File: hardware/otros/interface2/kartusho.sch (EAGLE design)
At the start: 9 parts, among them IC1 74HC164N, IC3 74HC32N, U1 AM29F040S

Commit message: 
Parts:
- removed U$1: IF2BUS, SPECTRUM:IF2BUS
- added U$2: IF2BUSMINI, SPECTRUM:IF2BUSMINI
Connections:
- net A0: now also U$2.A0; no longer U$1.A0
- net A1: now also U$2.A1; no longer U$1.A1
- net A10: now also U$2.A10; no longer U$1.A10
- net A11: now also U$2.A11; no longer U$1.A11
- net A12: now also U$2.A12; no longer U$1.A12
- net A13: now also U$2.A13; no longer U$1.A13
- net A14: now also U$2.A14; no longer U$1.A14
- net A15: now also U$2.A15; no longer U$1.A15
- net A2: now also U$2.A2; no longer U$1.A2
- net A3: now also U$2.A3; no longer U$1.A3
- net A4: now also U$2.A4; no longer U$1.A4
- net A5: now also U$2.A5; no longer U$1.A5
- net A6: now also U$2.A6; no longer U$1.A6
- net A7: now also U$2.A7; no longer U$1.A7
- net A8: now also U$2.A8; no longer U$1.A8
- net A9: now also U$2.A9; no longer U$1.A9
- net D0: now also U$2.D0; no longer U$1.D0
- net D1: now also U$2.D1; no longer U$1.D1
- net D2: now also U$2.D2; no longer U$1.D2
- net D3: now also U$2.D3; no longer U$1.D3
- net D4: now also U$2.D4; no longer U$1.D4
- net D5: now also U$2.D5; no longer U$1.D5
- net D6: now also U$2.D6; no longer U$1.D6
- net D7: now also U$2.D7; no longer U$1.D7
- net GND: now also U$2.GND; no longer U$1.GND
- net MREQ: now also U$2.MEMREQ; no longer U$1.MEMREQ
- net RD: now also U$2.RD; no longer U$1.RD
- net VCC: now also U$2.+5V, U$2.ROMCS; no longer U$1.+5V, U$1.ROMCS
- net WR: now also U$2.WR; no longer U$1.WR
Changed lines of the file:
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@@
 </classes>
 <parts>
-<part name="U$1" library="SPECTRUM" deviceset="IF2BUS" device=""/>
 <part name="C1" library="rcl" deviceset="C-EU" device="050-025X075" value="100nF"/>
 <part name="IC1" library="74xx-us" deviceset="74*164" device="N" technology="HC"/>
@@
 <part name="GND1" library="supply1" deviceset="GND" device=""/>
 <part name="P+1" library="supply1" deviceset="VCC" device=""/>
+<part name="U$2" library="SPECTRUM" deviceset="IF2BUSMINI" device=""/>
 </parts>
 <sheets>
@@
 </plain>
 <instances>
-<instance part="U$1" gate="G$1" x="-10.16" y="60.96"/>
 <instance part="C1" gate="G$1" x="10.16" y="93.98"/>
 <instance part="IC1" gate="A" x="50.8" y="48.26"/>
@@
 <instance part="GND1" gate="1" x="10.16" y="83.82"/>
 <instance part="P+1" gate="VCC" x="10.16" y="101.6"/>
+<instance part="U$2" gate="G$1" x="-10.16" y="60.96"/>
 </instances>
 <busses>
@@
 <wire x1="-15.24" y1="88.9" x2="-7.62" y2="88.9" width="0.1524" layer="91"/>
 <label x="-10.16" y="88.9" size="1.778" layer="95"/>
-<pinref part="U$1" gate="G$1" pin="D0"/>
+<pinref part="U$2" gate="G$1" pin="D0"/>
 </segment>
 <segment>
@@
 <wire x1="-15.24" y1="83.82" x2="-7.62" y2="83.82" width="0.1524" layer="91"/>
 <label x="-10.16" y="83.82" size="1.778" layer="95"/>
-<pinref part="U$1" gate="G$1" pin="D1"/>
+<pinref part="U$2" gate="G$1" pin="D1"/>
 </segment>
 <segment>
@@
 <wire x1="-15.24" y1="78.74" x2="-7.62" y2="78.74" width="0.1524" layer="91"/>
 <label x="-10.16" y="78.74" size="1.778" layer="95"/>
-<pinref part="U$1" gate="G$1" pin="D2"/>
+<pinref part="U$2" gate="G$1" pin="D2"/>
 </segment>
 <segment>
@@
 <wire x1="-15.24" y1="73.66" x2="-7.62" y2="73.66" width="0.1524" layer="91"/>
 <label x="-10.16" y="73.66" size="1.778" layer="95"/>
-<pinref part="U$1" gate="G$1" pin="D3"/>
+<pinref part="U$2" gate="G$1" pin="D3"/>
 </segment>
 <segment>
@@
 <wire x1="-15.24" y1="68.58" x2="-7.62" y2="68.58" width="0.1524" layer="91"/>
 <label x="-10.16" y="68.58" size="1.778" layer="95"/>
-<pinref part="U$1" gate="G$1" pin="D4"/>
+<pinref part="U$2" gate="G$1" pin="D4"/>
 </segment>
 <segment>
@@
 <wire x1="-15.24" y1="63.5" x2="-7.62" y2="63.5" width="0.1524" layer="91"/>
 <label x="-10.16" y="63.5" size="1.778" layer="95"/>
-<pinref part="U$1" gate="G$1" pin="D5"/>
+<pinref part="U$2" gate="G$1" pin="D5"/>
 </segment>
 <segment>
@@
 <wire x1="-15.24" y1="58.42" x2="-7.62" y2="58.42" width="0.1524" layer="91"/>
 <label x="-10.16" y="58.42" size="1.778" layer="95"/>
-<pinref part="U$1" gate="G$1" pin="D6"/>
+<pinref part="U$2" gate="G$1" pin="D6"/>
 </segment>
 <segment>
@@
 <wire x1="-15.24" y1="53.34" x2="-7.62" y2="53.34" width="0.1524" layer="91"/>
 <label x="-10.16" y="53.34" size="1.778" layer="95"/>
-<pinref part="U$1" gate="G$1" pin="D7"/>
+<pinref part="U$2" gate="G$1" pin="D7"/>
 </segment>
 <segment>
@@
 <wire x1="-53.34" y1="88.9" x2="-45.72" y2="88.9" width="0.1524" layer="91"/>
 <label x="-53.34" y="88.9" size="1.778" layer="95"/>
-<pinref part="U$1" gate="G$1" pin="A0"/>
+<pinref part="U$2" gate="G$1" pin="A0"/>
 </segment>
 <segment>
@@
 <wire x1="-53.34" y1="83.82" x2="-45.72" y2="83.82" width="0.1524" layer="91"/>
 <label x="-53.34" y="83.82" size="1.778" layer="95"/>
-<pinref part="U$1" gate="G$1" pin="A1"/>
+<pinref part="U$2" gate="G$1" pin="A1"/>
 </segment>
 <segment>
@@
 <wire x1="-53.34" y1="78.74" x2="-45.72" y2="78.74" width="0.1524" layer="91"/>
 <label x="-53.34" y="78.74" size="1.778" layer="95"/>
-<pinref part="U$1" gate="G$1" pin="A2"/>
+<pinref part="U$2" gate="G$1" pin="A2"/>
 </segment>
 <segment>
@@
 <wire x1="-53.34" y1="73.66" x2="-45.72" y2="73.66" width="0.1524" layer="91"/>
 <label x="-53.34" y="73.66" size="1.778" layer="95"/>
-<pinref part="U$1" gate="G$1" pin="A3"/>
+<pinref part="U$2" gate="G$1" pin="A3"/>
 </segment>
 <segment>
@@
 <wire x1="-53.34" y1="68.58" x2="-45.72" y2="68.58" width="0.1524" layer="91"/>
 <label x="-53.34" y="68.58" size="1.778" layer="95"/>
-<pinref part="U$1" gate="G$1" pin="A4"/>
+<pinref part="U$2" gate="G$1" pin="A4"/>
 </segment>
 <segment>
@@
 <wire x1="-53.34" y1="63.5" x2="-45.72" y2="63.5" width="0.1524" layer="91"/>
 <label x="-53.34" y="63.5" size="1.778" layer="95"/>
-<pinref part="U$1" gate="G$1" pin="A5"/>
+<pinref part="U$2" gate="G$1" pin="A5"/>
 </segment>
 <segment>
@@
 <wire x1="-53.34" y1="58.42" x2="-45.72" y2="58.42" width="0.1524" layer="91"/>
 <label x="-53.34" y="58.42" size="1.778" layer="95"/>
-<pinref part="U$1" gate="G$1" pin="A6"/>
+<pinref part="U$2" gate="G$1" pin="A6"/>
 </segment>
 <segment>
@@
 <wire x1="-53.34" y1="53.34" x2="-45.72" y2="53.34" width="0.1524" layer="91"/>
 <label x="-53.34" y="53.34" size="1.778" layer="95"/>
-<pinref part="U$1" gate="G$1" pin="A7"/>
+<pinref part="U$2" gate="G$1" pin="A7"/>
 </segment>
 <segment>
@@
 <wire x1="-53.34" y1="48.26" x2="-45.72" y2="48.26" width="0.1524" layer="91"/>
 <label x="-53.34" y="48.26" size="1.778" layer="95"/>
-<pinref part="U$1" gate="G$1" pin="A8"/>
+<pinref part="U$2" gate="G$1" pin="A8"/>
 </segment>
 <segment>
@@
 <wire x1="-53.34" y1="43.18" x2="-45.72" y2="43.18" width="0.1524" layer="91"/>
 <label x="-53.34" y="43.18" size="1.778" layer="95"/>
-<pinref part="U$1" gate="G$1" pin="A9"/>
+<pinref part="U$2" gate="G$1" pin="A9"/>
 </segment>
 <segment>
@@
 <wire x1="-53.34" y1="38.1" x2="-45.72" y2="38.1" width="0.1524" layer="91"/>
 <label x="-53.34" y="38.1" size="1.778" layer="95"/>
-<pinref part="U$1" gate="G$1" pin="A10"/>
+<pinref part="U$2" gate="G$1" pin="A10"/>
 </segment>
 <segment>
@@
 <wire x1="-53.34" y1="33.02" x2="-45.72" y2="33.02" width="0.1524" layer="91"/>
 <label x="-53.34" y="33.02" size="1.778" layer="95"/>
-<pinref part="U$1" gate="G$1" pin="A11"/>
+<pinref part="U$2" gate="G$1" pin="A11"/>
 </segment>
 <segment>
@@
 <wire x1="-53.34" y1="27.94" x2="-45.72" y2="27.94" width="0.1524" layer="91"/>
 <label x="-53.34" y="27.94" size="1.778" layer="95"/>
-<pinref part="U$1" gate="G$1" pin="A12"/>
+<pinref part="U$2" gate="G$1" pin="A12"/>
 </segment>
 <segment>
@@
 <wire x1="-53.34" y1="22.86" x2="-45.72" y2="22.86" width="0.1524" layer="91"/>
 <label x="-53.34" y="22.86" size="1.778" layer="95"/>
-<pinref part="U$1" gate="G$1" pin="A13"/>
+<pinref part="U$2" gate="G$1" pin="A13"/>
 </segment>
 <segment>
@@
 <wire x1="-53.34" y1="17.78" x2="-45.72" y2="17.78" width="0.1524" layer="91"/>
 <label x="-53.34" y="17.78" size="1.778" layer="95"/>
-<pinref part="U$1" gate="G$1" pin="A14"/>
+<pinref part="U$2" gate="G$1" pin="A14"/>
 </segment>
 <segment>
@@
 <wire x1="-53.34" y1="12.7" x2="-45.72" y2="12.7" width="0.1524" layer="91"/>
 <label x="-53.34" y="12.7" size="1.778" layer="95"/>
-<pinref part="U$1" gate="G$1" pin="A15"/>
+<pinref part="U$2" gate="G$1" pin="A15"/>
 </segment>
 <segment>
@@
 <wire x1="-15.24" y1="48.26" x2="-7.62" y2="48.26" width="0.1524" layer="91"/>
 <label x="-10.16" y="48.26" size="1.778" layer="95"/>
-<pinref part="U$1" gate="G$1" pin="MEMREQ"/>
+<pinref part="U$2" gate="G$1" pin="MEMREQ"/>
 </segment>
 <segment>
@@
 <wire x1="-15.24" y1="33.02" x2="-7.62" y2="33.02" width="0.1524" layer="91"/>
 <label x="-10.16" y="33.02" size="1.778" layer="95"/>
-<pinref part="U$1" gate="G$1" pin="GND"/>
+<pinref part="U$2" gate="G$1" pin="GND"/>
 </segment>
 <segment>
@@
 <wire x1="-7.62" y1="38.1" x2="-5.08" y2="38.1" width="0.1524" layer="91"/>
 <junction x="-7.62" y="38.1"/>
-<pinref part="U$1" gate="G$1" pin="+5V"/>
-<pinref part="U$1" gate="G$1" pin="ROMCS"/>
+<pinref part="U$2" gate="G$1" pin="+5V"/>
+<pinref part="U$2" gate="G$1" pin="ROMCS"/>
 </segment>
 <segment>
@@
 <wire x1="-15.24" y1="27.94" x2="-7.62" y2="27.94" width="0.1524" layer="91"/>
 <label x="-10.16" y="27.94" size="1.778" layer="95"/>
-<pinref part="U$1" gate="G$1" pin="RD"/>
+<pinref part="U$2" gate="G$1" pin="RD"/>
 </segment>
 </net>
@@
 <wire x1="-15.24" y1="22.86" x2="-7.62" y2="22.86" width="0.1524" layer="91"/>
 <label x="-10.16" y="22.86" size="1.778" layer="95"/>
-<pinref part="U$1" gate="G$1" pin="WR"/>
-</segment>
-<segment>
+<pinref part="U$2" gate="G$1" pin="WR"/>
+</segment>
+<segment>

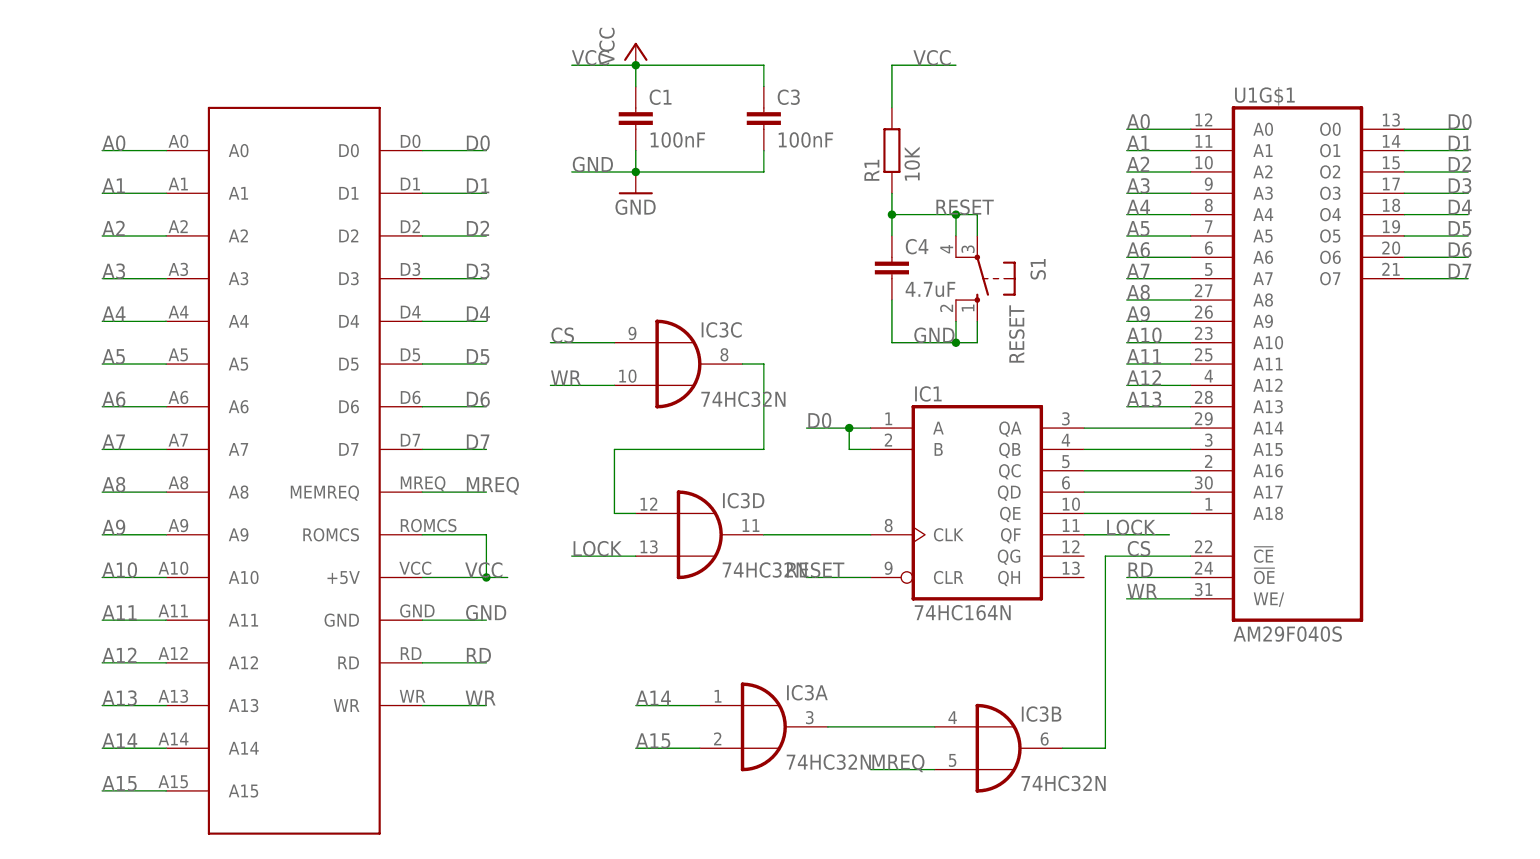
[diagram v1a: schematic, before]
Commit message: 
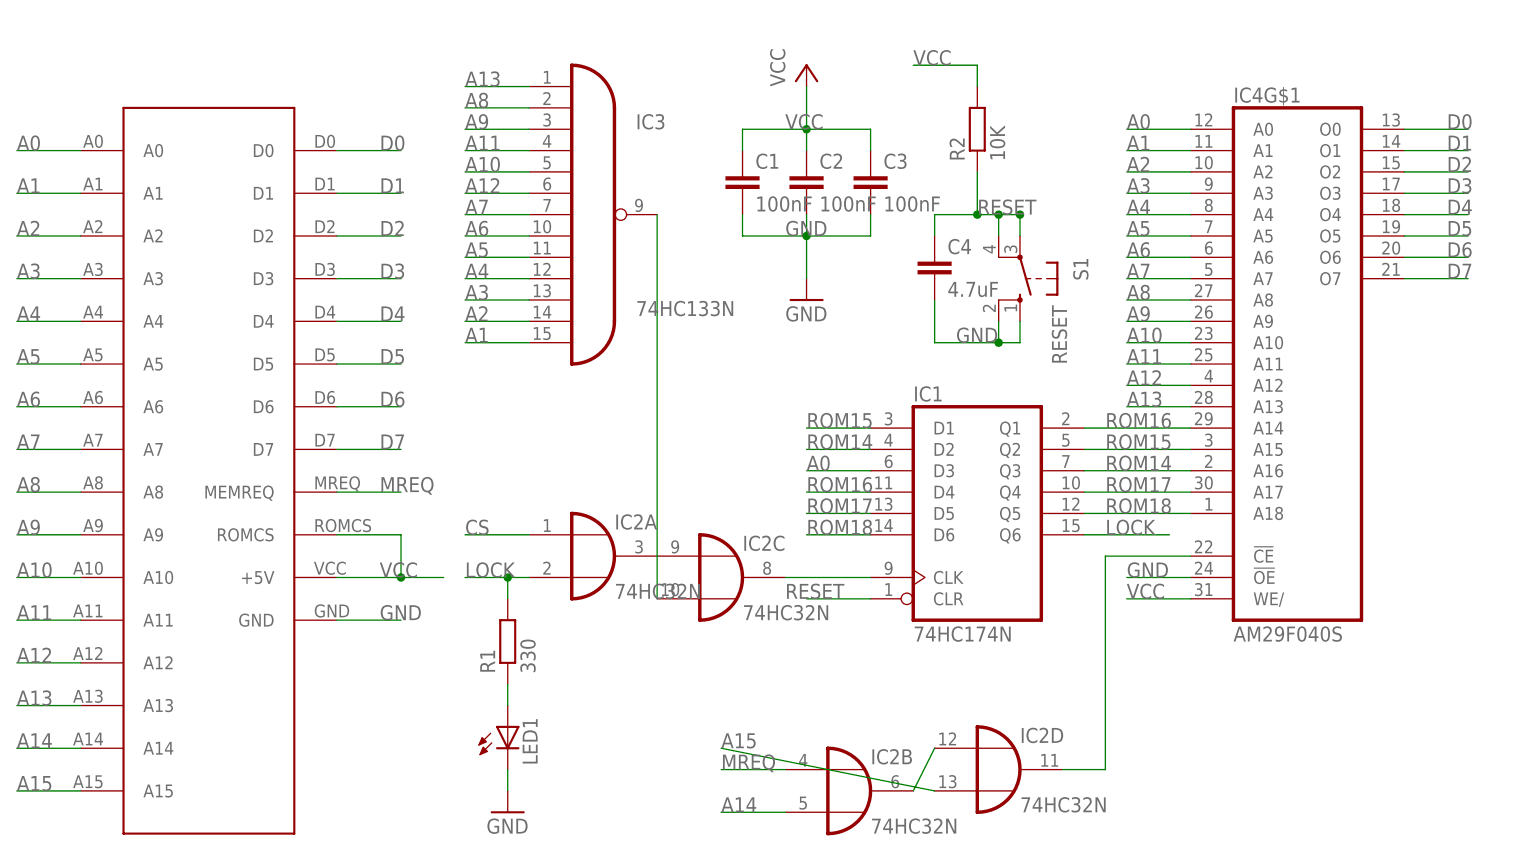
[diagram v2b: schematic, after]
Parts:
- removed U$2: IF2BUSMINI, SPECTRUM:IF2BUSMINI
- added C2: 100nF, rcl:C-EU025-025X050
- added IC2: 74HC32N, 74xx-eu:74HC32N
- added LED1: (no value), led:LED3MM
- added R2: 10K, rcl:R-EU_0204/7
- added U$1: IF2BUS, SPECTRUM:IF2BUS
- C1, C3, C4: device rcl:C-EU050-025X075 -> rcl:C-EU025-025X050
- IC1: value 74HC164N -> 74HC174N; device 74xx-us:74HC164N -> 74xx-eu:74HC174N
- IC3: value 74HC32N -> 74HC133N; device 74xx-eu:74HC32N -> 74xx-eu:74HC133N
- R1: value 10K -> 330
- renumbered U1 to IC4
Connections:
- removed net N$10: IC1A.CLK, IC3D.O
- removed net N$11: IC3C.O, IC3D.I0
- removed net N$5: IC1A.QB, IC4G$1.A15
- removed net N$6: IC1A.QA, IC4G$1.A14
- removed net RD: IC4G$1.!OE, U$2.RD
- removed net WR: IC3C.I1, IC4G$1.WE/, U$2.WR
- new net N$1: IC1A.CLK, IC2C.O
- new net ROM14: IC1A.D2, IC1A.Q3, IC4G$1.A16
- new net ROM15: IC1A.D1, IC1A.Q2, IC4G$1.A15
- new net ROM16: IC1A.D4, IC1A.Q1, IC4G$1.A14
- new net ROM17: IC1A.D5, IC1A.Q4, IC4G$1.A17
- new net ROM18: IC1A.D6, IC1A.Q5, IC4G$1.A18
- net A0: now also IC1A.D3, U$1.A0; no longer U$2.A0
- net A1: now also IC3A.I12, U$1.A1; no longer U$2.A1
- net A10: now also IC3A.I4, U$1.A10; no longer U$2.A10
- net A11: now also IC3A.I3, U$1.A11; no longer U$2.A11
- net A12: now also IC3A.I5, U$1.A12; no longer U$2.A12
- net A13: now also IC3A.I0, U$1.A13; no longer U$2.A13
- net A14: now also IC2B.I1, U$1.A14; no longer IC3A.I0, U$2.A14
- net A15: now also IC2D.I1, U$1.A15; no longer IC3A.I1, U$2.A15
- net A2: now also IC3A.I11, U$1.A2; no longer U$2.A2
- net A3: now also IC3A.I10, U$1.A3; no longer U$2.A3
- net A4: now also IC3A.I9, U$1.A4; no longer U$2.A4
- net A5: now also IC3A.I8, U$1.A5; no longer U$2.A5
- net A6: now also IC3A.I7, U$1.A6; no longer U$2.A6
- net A7: now also IC3A.I6, U$1.A7; no longer U$2.A7
- net A8: now also IC3A.I1, U$1.A8; no longer U$2.A8
- net A9: now also IC3A.I2, U$1.A9; no longer U$2.A9
- net CS: now also IC2A.I0, IC2D.O; no longer IC3B.O, IC3C.I0
- net D0: now also U$1.D0; no longer IC1A.A, IC1A.B, U$2.D0
- net D1: now also U$1.D1; no longer U$2.D1
- net D2: now also U$1.D2; no longer U$2.D2
- net D3: now also U$1.D3; no longer U$2.D3
- net D4: now also U$1.D4; no longer U$2.D4
- net D5: now also U$1.D5; no longer U$2.D5
- net D6: now also U$1.D6; no longer U$2.D6
- net D7: now also U$1.D7; no longer U$2.D7
- net GND: now also C2.2, IC4G$1.!OE, LED1.C, U$1.GND; no longer U$2.GND
- net LOCK: now also IC1A.Q6, IC2A.I1, R1.2; no longer IC1A.QF, IC3D.I1
- net MREQ: now also IC2B.I0, U$1.MEMREQ; no longer IC3B.I1, U$2.MEMREQ
- net N$2: now also IC2B.O, IC2D.I0; no longer IC1A.QE, IC4G$1.A18
- net N$3: now also IC2A.O, IC2C.I0; no longer IC1A.QD, IC4G$1.A17
- net N$4: now also IC2C.I1, IC3A.O; no longer IC1A.QC, IC4G$1.A16
- net N$7: now also LED1.A, R1.1; no longer IC3A.O, IC3B.I0
- net RESET: now also R2.1; no longer R1.1
- net VCC: now also C2.1, IC4G$1.WE/, R2.2, U$1.+5V, U$1.ROMCS; no longer R1.2, U$2.+5V, U$2.ROMCS
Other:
- moved on the sheet: C1, C3, C4, R1, S1

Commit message: 
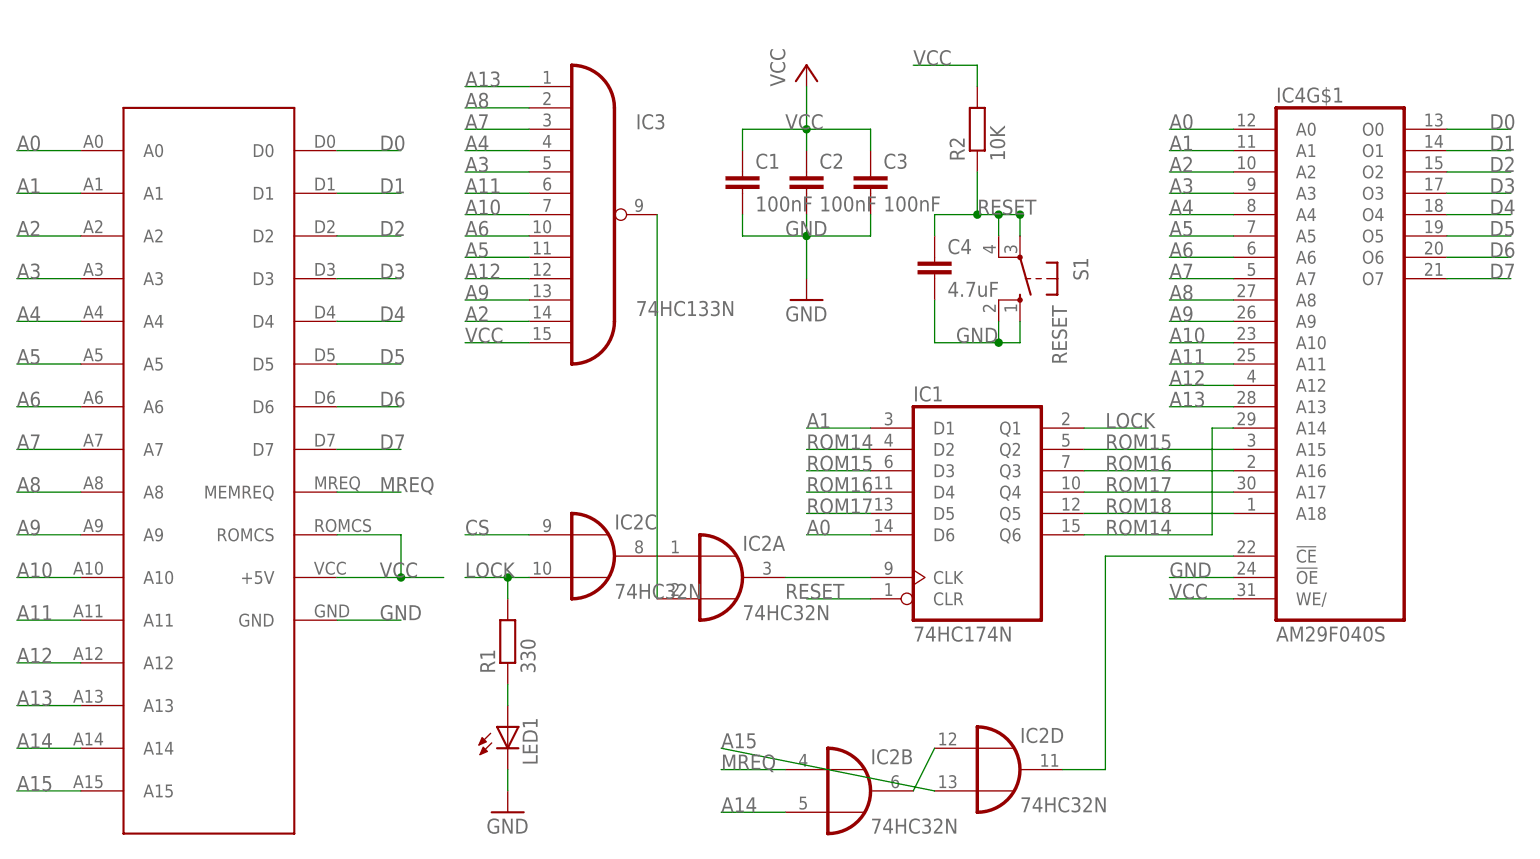
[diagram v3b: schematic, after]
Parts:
- C3: device rcl:C-EU025-025X050 -> rcl:C-EU050-025X075
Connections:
- net A0: now also IC1A.D6; no longer IC1A.D3
- net A1: now also IC1A.D1; no longer IC3A.I12
- net A10: now also IC3A.I6; no longer IC3A.I4
- net A11: now also IC3A.I5; no longer IC3A.I3
- net A12: now also IC3A.I9; no longer IC3A.I5
- net A3: now also IC3A.I4; no longer IC3A.I10
- net A4: now also IC3A.I3; no longer IC3A.I9
- net A7: now also IC3A.I2; no longer IC3A.I6
- net A9: now also IC3A.I10; no longer IC3A.I2
- net CS: now also IC2C.I0; no longer IC2A.I0
- net LOCK: now also IC1A.Q1, IC2C.I1; no longer IC1A.Q6, IC2A.I1
- net N$1: now also IC2A.O; no longer IC2C.O
- net N$3: now also IC2A.I0, IC2C.O; no longer IC2A.O, IC2C.I0
- net N$4: now also IC2A.I1; no longer IC2C.I1
- net ROM14: now also IC1A.Q6, IC4G$1.A14; no longer IC1A.Q3, IC4G$1.A16
- net ROM15: now also IC1A.D3; no longer IC1A.D1
- net ROM16: now also IC1A.Q3, IC4G$1.A16; no longer IC1A.Q1, IC4G$1.A14
- net ROM18: no longer IC1A.D6
- net VCC: now also IC3A.I12
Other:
- moved on the sheet: IC2A, IC2C, IC4G$1

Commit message: 
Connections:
- net A3: now also IC3A.I10; no longer IC3A.I4
- net A9: now also IC3A.I4; no longer IC3A.I10
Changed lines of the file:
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@@
 </segment>
 <segment>
-<wire x1="-10.16" y1="86.36" x2="-2.54" y2="86.36" width="0.1524" layer="91"/>
-<pinref part="IC3" gate="A" pin="I4"/>
-<label x="-10.16" y="86.36" size="1.778" layer="95"/>
+<wire x1="-10.16" y1="71.12" x2="-2.54" y2="71.12" width="0.1524" layer="91"/>
+<pinref part="IC3" gate="A" pin="I10"/>
+<label x="-10.16" y="71.12" size="1.778" layer="95"/>
 </segment>
 </net>
@@
 </segment>
 <segment>
-<wire x1="-10.16" y1="71.12" x2="-2.54" y2="71.12" width="0.1524" layer="91"/>
-<pinref part="IC3" gate="A" pin="I10"/>
-<label x="-10.16" y="71.12" size="1.778" layer="95"/>
+<wire x1="-10.16" y1="86.36" x2="-2.54" y2="86.36" width="0.1524" layer="91"/>
+<pinref part="IC3" gate="A" pin="I4"/>
+<label x="-10.16" y="86.36" size="1.778" layer="95"/>
 </segment>
 </net>
